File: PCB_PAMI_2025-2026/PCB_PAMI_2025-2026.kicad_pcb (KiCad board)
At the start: 2 copper layers, 125 x 84 mm, 63 parts, among them J1 BAU, J10 MOTOR 4, J11 COMM_inter_mcu, J12 USB_C_Receptacle_USB2.0_16P, J13 BOOST_OUT, J2 BAT+, J3 VIN_Connector, J4 BAT-, J6 BOOST_IN, J7 MOTOR 3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

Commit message: ajout des via pour mieux relier les plans de masses
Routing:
- net GND: track 41.6 -> 58.7 mm, vias 3 -> 24

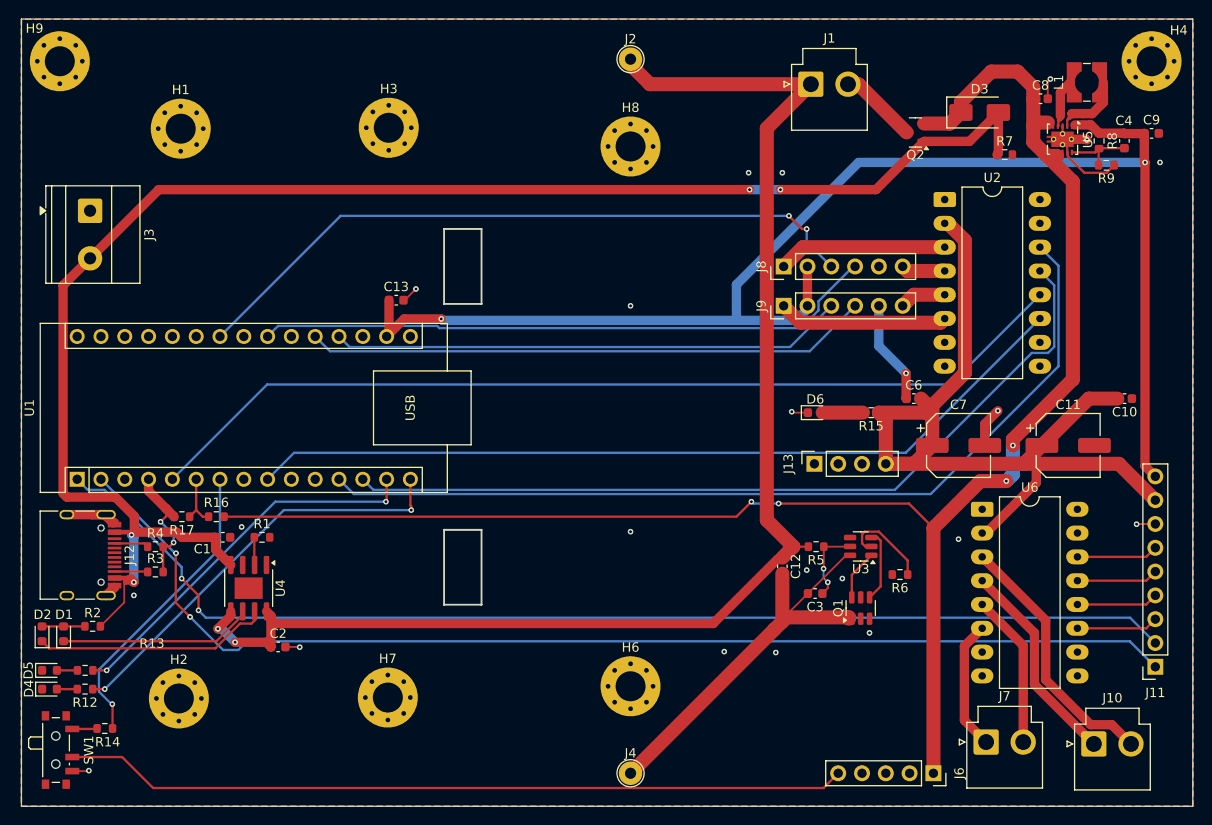
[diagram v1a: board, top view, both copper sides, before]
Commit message: correction schéma driver + rajout via gnd
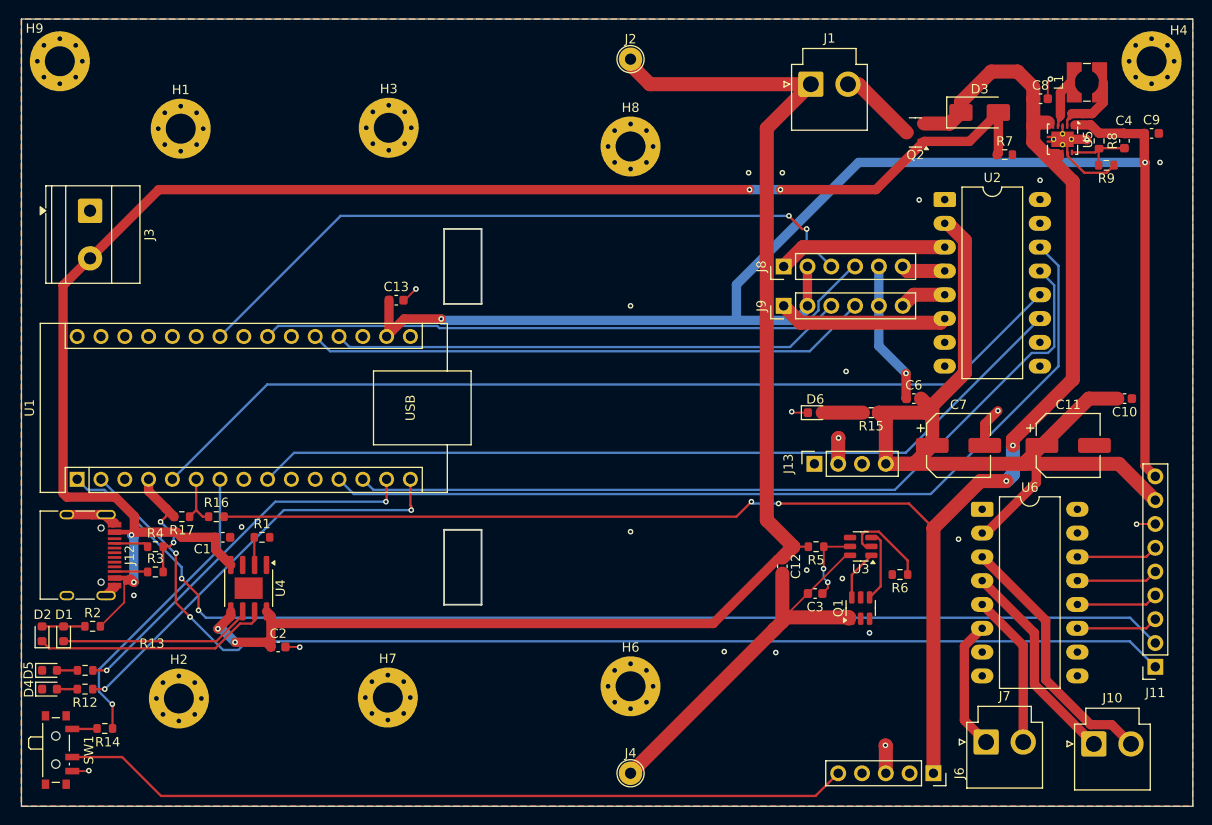
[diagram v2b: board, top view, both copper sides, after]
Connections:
- U2 pad 16: unconnected-(U2-FLT-Pad16) -> GND
- U2 pad 9: GND -> unconnected-(U2-FLT-Pad9)
- U6 pad 16: unconnected-(U6-FLT-Pad16) -> GND
- U6 pad 9: GND -> unconnected-(U6-FLT-Pad9)
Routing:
- net GND: track 58.7 -> 68.7 mm, vias 24 -> 29
- net Net-(J6-Pin_5): track 83.8 -> 84.5 mm
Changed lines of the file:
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@@
 	(net 67 "unconnected-(U2-AISEN-Pad7)")
 	(net 68 "unconnected-(U2-BISEN-Pad8)")
-	(net 69 "unconnected-(U2-FLT-Pad16)")
-	(net 70 "unconnected-(U2-VMM-Pad10)")
-	(net 71 "unconnected-(U2-SLP-Pad15)")
+	(net 69 "unconnected-(U2-FLT-Pad9)")
+	(net 70 "unconnected-(U2-SLP-Pad10)")
+	(net 71 "unconnected-(U2-VMM-Pad15)")
 	(net 72 "unconnected-(U3-NC-Pad4)")
 	(net 73 "unconnected-(U6-BISEN-Pad8)")
-	(net 74 "unconnected-(U6-VMM-Pad10)")
-	(net 75 "unconnected-(U6-SLP-Pad15)")
+	(net 74 "unconnected-(U6-SLP-Pad10)")
+	(net 75 "unconnected-(U6-FLT-Pad9)")
 	(net 76 "/DOUT1")
 	(net 77 "/DOUT2")
-	(net 78 "unconnected-(U6-FLT-Pad16)")
+	(net 78 "unconnected-(U6-VMM-Pad15)")
 	(net 79 "unconnected-(U6-AISEN-Pad7)")
 	(net 80 "Net-(J12-CC1)")
@@
 			(layers "*.Cu" "*.Mask")
 			(remove_unused_layers no)
-			(net 2 "GND")
-			(pinfunction "GND")
-			(pintype "power_in")
+			(net 75 "unconnected-(U6-FLT-Pad9)")
+			(pinfunction "FLT")
+			(pintype "passive+no_connect")
 		)
 		(pad "10" thru_hole oval
@@
 			(layers "*.Cu" "*.Mask")
 			(remove_unused_layers no)
-			(net 74 "unconnected-(U6-VMM-Pad10)")
-			(pinfunction "VMM")
-			(pintype "power_in+no_connect")
+			(net 74 "unconnected-(U6-SLP-Pad10)")
+			(pinfunction "SLP")
+			(pintype "passive+no_connect")
 		)
 		(pad "11" thru_hole oval
@@
 			(remove_unused_layers no)
 			(net 35 "/DIN2")
-			(pinfunction "BIN1")
+			(pinfunction "AIN1")
 			(pintype "passive")
 		)
@@
 			(remove_unused_layers no)
 			(net 34 "/DIN1")
-			(pinfunction "BIN2")
+			(pinfunction "AIN2")
 			(pintype "passive")
 		)
@@
 			(remove_unused_layers no)
 			(net 33 "/CIN2")
-			(pinfunction "AIN2")
+			(pinfunction "BIN2")
 			(pintype "passive")
 		)
@@
 			(remove_unused_layers no)
 			(net 30 "/CIN1")
-			(pinfunction "AIN1")
+			(pinfunction "BIN1")
 			(pintype "passive")
 		)
@@
 			(layers "*.Cu" "*.Mask")
 			(remove_unused_layers no)
-			(net 75 "unconnected-(U6-SLP-Pad15)")
-			(pinfunction "SLP")
-			(pintype "passive+no_connect")
+			(net 78 "unconnected-(U6-VMM-Pad15)")
+			(pinfunction "VMM")
+			(pintype "power_in+no_connect")
 		)
 		(pad "16" thru_hole oval
@@
 			(layers "*.Cu" "*.Mask")
 			(remove_unused_layers no)
-			(net 78 "unconnected-(U6-FLT-Pad16)")
-			(pinfunction "FLT")
-			(pintype "passive+no_connect")
+			(net 2 "GND")
+			(pinfunction "GND")
+			(pintype "power_in")
 		)
 		(embedded_fonts no)
@@
 			(layers "*.Cu" "*.Mask")
 			(remove_unused_layers no)
-			(net 2 "GND")
-			(pinfunction "GND")
-			(pintype "power_in")
+			(net 69 "unconnected-(U2-FLT-Pad9)")
+			(pinfunction "FLT")
+			(pintype "passive+no_connect")
 		)
 		(pad "10" thru_hole oval
@@
 			(layers "*.Cu" "*.Mask")
 			(remove_unused_layers no)
-			(net 70 "unconnected-(U2-VMM-Pad10)")
-			(pinfunction "VMM")
-			(pintype "power_in+no_connect")
+			(net 70 "unconnected-(U2-SLP-Pad10)")
+			(pinfunction "SLP")
+			(pintype "passive+no_connect")
 		)
 		(pad "11" thru_hole oval
@@
 			(remove_unused_layers no)
 			(net 63 "/BIN1")
-			(pinfunction "BIN1")
+			(pinfunction "AIN1")
 			(pintype "passive")
 		)
@@
 			(remove_unused_layers no)
 			(net 65 "/BIN2")
-			(pinfunction "BIN2")
+			(pinfunction "AIN2")
 			(pintype "passive")
 		)
@@
 			(remove_unused_layers no)
 			(net 55 "/AIN2")
-			(pinfunction "AIN2")
+			(pinfunction "BIN2")
 			(pintype "passive")
 		)
@@
 			(remove_unused_layers no)
 			(net 57 "/AIN1")
-			(pinfunction "AIN1")
+			(pinfunction "BIN1")
 			(pintype "passive")
 		)
@@
 			(layers "*.Cu" "*.Mask")
 			(remove_unused_layers no)
-			(net 71 "unconnected-(U2-SLP-Pad15)")
-			(pinfunction "SLP")
-			(pintype "passive+no_connect")
+			(net 71 "unconnected-(U2-VMM-Pad15)")
+			(pinfunction "VMM")
+			(pintype "power_in+no_connect")
 		)
 		(pad "16" thru_hole oval
@@
 			(layers "*.Cu" "*.Mask")
 			(remove_unused_layers no)
-			(net 69 "unconnected-(U2-FLT-Pad16)")
-			(pinfunction "FLT")
-			(pintype "passive+no_connect")
+			(net 2 "GND")
+			(pinfunction "GND")
+			(pintype "power_in")
 		)
 		(embedded_fonts no)
@@
 	)
 	(segment
+		(start 137.16 60.96)
+		(end 137.16 58.24)
+		(width 1.5)
+		(layer "F.Cu")
+		(net 2)
+	)
+	(segment
 		(start 55.43 93.75)
 		(end 57.15 93.75)
@@
 	)
 	(segment
+		(start 142.24 93.98)
+		(end 142.24 91.04)
+		(width 1.5)
+		(layer "F.Cu")
+		(net 2)
+	)
+	(segment
 		(start 59.03 66.38)
 		(end 59.03 66.535)
@@
 	)
 	(segment
+		(start 142.24 91.04)
+		(end 142.2 91)
+		(width 1.5)
+		(layer "F.Cu")
+		(net 2)
+	)
+	(segment
 		(start 161.1 26.9)
 		(end 161.524264 26.9)
@@
 		(net 2)
 	)
+	(segment
+		(start 137.16 58.24)
+		(end 137.2 58.2)
+		(width 1.5)
+		(layer "F.Cu")
+		(net 2)
+	)
 	(via
 		(at 73.5 67.7)
@@
 	)
 	(via
+		(at 137.2 58.2)
+		(size 0.6)
+		(drill 0.3)
+		(layers "F.Cu" "B.Cu")
+		(net 2)
+	)
+	(via
 		(at 115 44.1)
 		(size 0.6)
@@
 	)
 	(via
+		(at 142.2 91)
+		(size 0.6)
+		(drill 0.3)
+		(layers "F.Cu" "B.Cu")
+		(net 2)
+	)
+	(via
+		(at 145.8 32.8)
+		(size 0.6)
+		(drill 0.3)
+		(layers "F.Cu" "B.Cu")
+		(free yes)
+		(net 2)
+	)
+	(via
+		(at 158.7 30.7)
+		(size 0.6)
+		(drill 0.3)
+		(layers "F.Cu" "B.Cu")
+		(free yes)
+		(net 2)
+	)
+	(via
 		(at 57.2 93.7)
 		(size 0.6)
@@
 	)
 	(via
+		(at 138 51.1)
+		(size 0.6)
+		(drill 0.3)
+		(layers "F.Cu" "B.Cu")
+		(free yes)
+		(net 2)
+	)
+	(via
 		(at 92.1 42.3)
 		(size 0.6)
@@
 	(segment
 		(start 141.5 44.1)
+		(end 141.5 39.9)
+		(width 1)
+		(layer "B.Cu")
+		(net 2)
+	)
+	(segment
+		(start 141.5 44.1)
 		(end 141.5 48.4)
 		(width 1)
@@
 	)
 	(segment
-		(start 135.584 95.556)
-		(end 137.16 93.98)
+		(start 64.9 96.4)
+		(end 134.74 96.4)
 		(width 0.25)
 		(layer "F.Cu")
@@
 	)
 	(segment
-		(start 64.056 95.556)
-		(end 135.584 95.556)
+		(start 55.43 92.25)
+		(end 60.75 92.25)
 		(width 0.25)
 		(layer "F.Cu")
@@
 	)
 	(segment
-		(start 55.43 92.25)
-		(end 60.75 92.25)
+		(start 134.74 96.4)
+		(end 137.16 93.98)
 		(width 0.25)
 		(layer "F.Cu")
@@
 	(segment
 		(start 60.75 92.25)
-		(end 64.056 95.556)
+		(end 64.9 96.4)
 		(width 0.25)
 		(layer "F.Cu")
